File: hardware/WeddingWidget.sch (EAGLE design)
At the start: 7 parts, among them J1 AVR_SPI_PRG_6NS, SW1 EVQQ2, SW2 EVQQ2

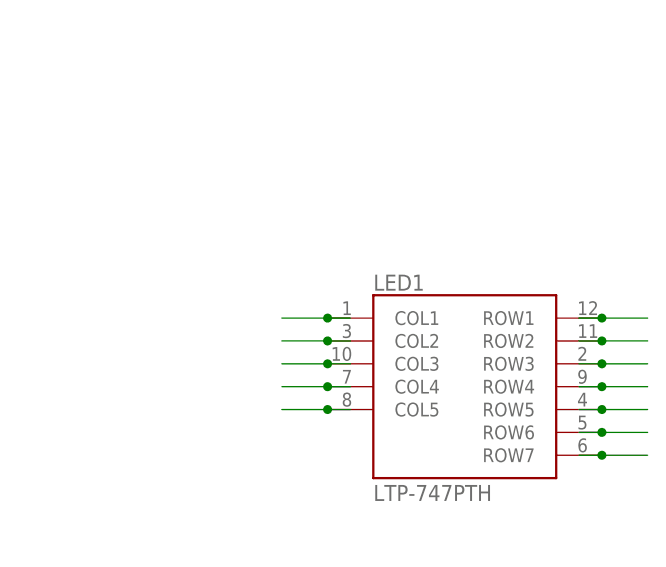
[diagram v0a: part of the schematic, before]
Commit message: added battery holder and bottom ground plane
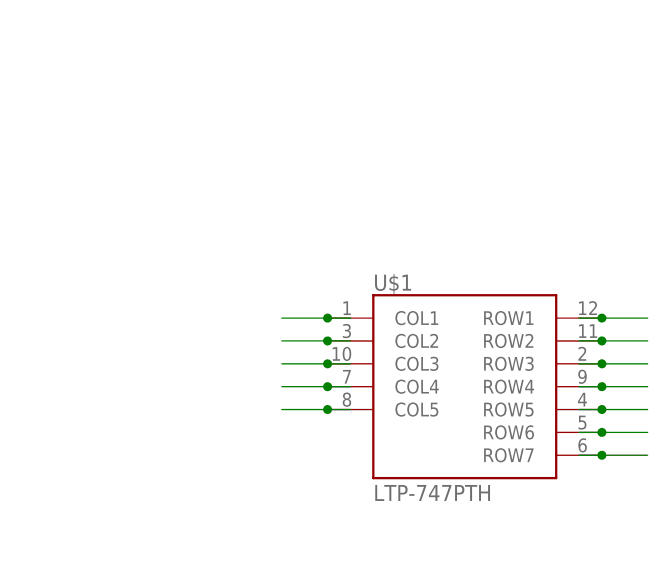
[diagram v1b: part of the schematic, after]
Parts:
- BAT1: device SparkFun:BATTERY12MM -> rxtx-labs:BATTERY12MM
- renumbered LED1 to U$1
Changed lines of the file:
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@@
 <part name="SW1" library="adafruit" deviceset="EVQQ2" device=""/>
 <part name="J1" library="SparkFun" deviceset="AVR_SPI_PRG_6" device="NS"/>
-<part name="BAT1" library="SparkFun" deviceset="BATTERY" device="12MM"/>
-<part name="LED1" library="LiteOn-LED-Matrix" deviceset="LTP-747" device="PTH"/>
 <part name="SW2" library="adafruit" deviceset="EVQQ2" device=""/>
+<part name="BAT1" library="rxtx-labs" deviceset="BATTERY" device="12MM"/>
+<part name="U$1" library="LiteOn-LED-Matrix" deviceset="LTP-747" device="PTH"/>
 </parts>
 <sheets>
@@
 <instance part="SW1" gate="G$1" x="25.4" y="193.04" rot="R270"/>
 <instance part="J1" gate="G$1" x="83.82" y="236.22"/>
+<instance part="SW2" gate="G$1" x="25.4" y="167.64" rot="R270"/>
 <instance part="BAT1" gate="G$1" x="33.02" y="226.06"/>
-<instance part="LED1" gate="G$1" x="182.88" y="175.26"/>
-<instance part="SW2" gate="G$1" x="25.4" y="167.64" rot="R270"/>
+<instance part="U$1" gate="G$1" x="182.88" y="175.26"/>
 </instances>
 <busses>
@@
 <segment>
 <wire x1="170.18" y1="182.88" x2="167.64" y2="182.88" width="0.1524" layer="91"/>
-<pinref part="LED1" gate="G$1" pin="COL1"/>
+<pinref part="U$1" gate="G$1" pin="COL1"/>
 <wire x1="167.64" y1="182.88" x2="162.56" y2="182.88" width="0.1524" layer="91"/>
 <junction x="167.64" y="182.88"/>
@@
 <segment>
 <wire x1="170.18" y1="180.34" x2="167.64" y2="180.34" width="0.1524" layer="91"/>
-<pinref part="LED1" gate="G$1" pin="COL2"/>
+<pinref part="U$1" gate="G$1" pin="COL2"/>
 <wire x1="167.64" y1="180.34" x2="162.56" y2="180.34" width="0.1524" layer="91"/>
 <junction x="167.64" y="180.34"/>
@@
 <segment>
 <wire x1="170.18" y1="177.8" x2="167.64" y2="177.8" width="0.1524" layer="91"/>
-<pinref part="LED1" gate="G$1" pin="COL3"/>
+<pinref part="U$1" gate="G$1" pin="COL3"/>
 <wire x1="167.64" y1="177.8" x2="162.56" y2="177.8" width="0.1524" layer="91"/>
 <junction x="167.64" y="177.8"/>
@@
 <segment>
 <wire x1="170.18" y1="175.26" x2="167.64" y2="175.26" width="0.1524" layer="91"/>
-<pinref part="LED1" gate="G$1" pin="COL4"/>
+<pinref part="U$1" gate="G$1" pin="COL4"/>
 <wire x1="167.64" y1="175.26" x2="162.56" y2="175.26" width="0.1524" layer="91"/>
 <junction x="167.64" y="175.26"/>
@@
 <segment>
 <wire x1="170.18" y1="172.72" x2="167.64" y2="172.72" width="0.1524" layer="91"/>
-<pinref part="LED1" gate="G$1" pin="COL5"/>
+<pinref part="U$1" gate="G$1" pin="COL5"/>
 <wire x1="167.64" y1="172.72" x2="162.56" y2="172.72" width="0.1524" layer="91"/>
 <junction x="167.64" y="172.72"/>
@@
 <segment>
 <wire x1="195.58" y1="182.88" x2="198.12" y2="182.88" width="0.1524" layer="91"/>
-<pinref part="LED1" gate="G$1" pin="ROW1"/>
+<pinref part="U$1" gate="G$1" pin="ROW1"/>
 <wire x1="198.12" y1="182.88" x2="203.2" y2="182.88" width="0.1524" layer="91"/>
 <junction x="198.12" y="182.88"/>
@@
 <segment>
 <wire x1="195.58" y1="180.34" x2="198.12" y2="180.34" width="0.1524" layer="91"/>
-<pinref part="LED1" gate="G$1" pin="ROW2"/>
+<pinref part="U$1" gate="G$1" pin="ROW2"/>
 <wire x1="198.12" y1="180.34" x2="203.2" y2="180.34" width="0.1524" layer="91"/>
 <junction x="198.12" y="180.34"/>
@@
 <segment>
 <wire x1="195.58" y1="177.8" x2="198.12" y2="177.8" width="0.1524" layer="91"/>
-<pinref part="LED1" gate="G$1" pin="ROW3"/>
+<pinref part="U$1" gate="G$1" pin="ROW3"/>
 <wire x1="198.12" y1="177.8" x2="203.2" y2="177.8" width="0.1524" layer="91"/>
 <junction x="198.12" y="177.8"/>
@@
 <segment>
 <wire x1="195.58" y1="175.26" x2="198.12" y2="175.26" width="0.1524" layer="91"/>
-<pinref part="LED1" gate="G$1" pin="ROW4"/>
+<pinref part="U$1" gate="G$1" pin="ROW4"/>
 <wire x1="198.12" y1="175.26" x2="203.2" y2="175.26" width="0.1524" layer="91"/>
 <junction x="198.12" y="175.26"/>
@@
 <segment>
 <wire x1="195.58" y1="172.72" x2="198.12" y2="172.72" width="0.1524" layer="91"/>
-<pinref part="LED1" gate="G$1" pin="ROW5"/>
+<pinref part="U$1" gate="G$1" pin="ROW5"/>
 <wire x1="198.12" y1="172.72" x2="203.2" y2="172.72" width="0.1524" layer="91"/>
 <junction x="198.12" y="172.72"/>
@@
 <segment>
 <wire x1="195.58" y1="170.18" x2="198.12" y2="170.18" width="0.1524" layer="91"/>
-<pinref part="LED1" gate="G$1" pin="ROW6"/>
+<pinref part="U$1" gate="G$1" pin="ROW6"/>
 <wire x1="198.12" y1="170.18" x2="203.2" y2="170.18" width="0.1524" layer="91"/>
 <junction x="198.12" y="170.18"/>
@@
 <segment>
 <wire x1="195.58" y1="167.64" x2="198.12" y2="167.64" width="0.1524" layer="91"/>
-<pinref part="LED1" gate="G$1" pin="ROW7"/>
+<pinref part="U$1" gate="G$1" pin="ROW7"/>
 <wire x1="198.12" y1="167.64" x2="203.2" y2="167.64" width="0.1524" layer="91"/>
 <junction x="198.12" y="167.64"/>

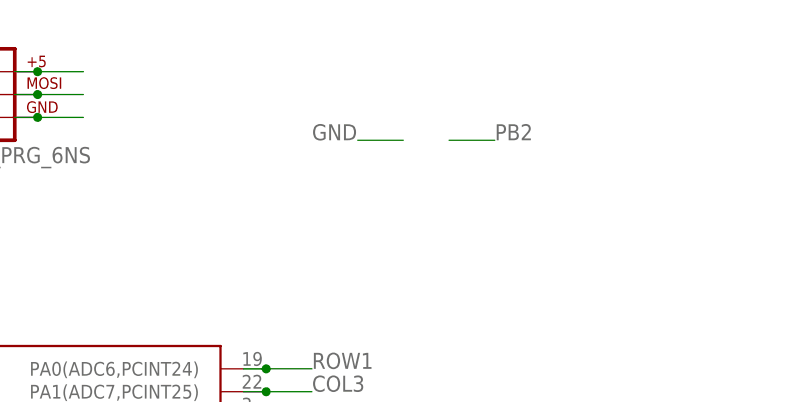
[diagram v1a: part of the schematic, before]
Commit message: Hand routed all traces. Ready for prototype boards to be produced.
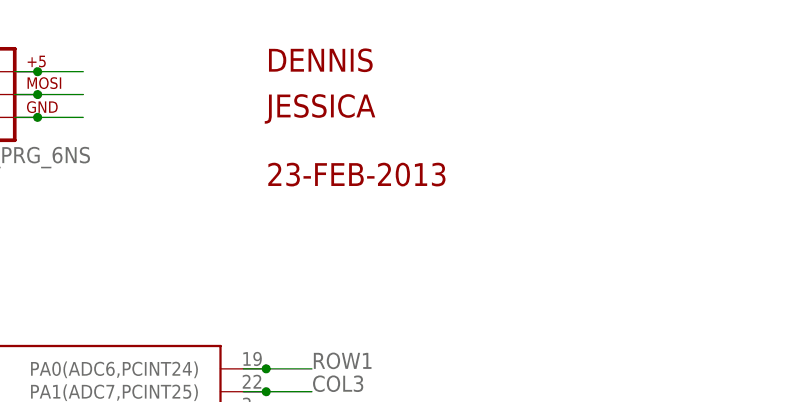
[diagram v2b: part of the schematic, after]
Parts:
- added U$2: DENNIS, rxtx-labs:DENNIS
- added U$3: JESSICA, rxtx-labs:JESSICA
- added U$4: 23FEB2013, rxtx-labs:23FEB2013
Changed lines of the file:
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@@
 <part name="BAT1" library="rxtx-labs" deviceset="BATTERY" device="12MM"/>
 <part name="U$1" library="LiteOn-LED-Matrix" deviceset="LTP-747" device="PTH"/>
+<part name="U$2" library="rxtx-labs" deviceset="DENNIS" device=""/>
+<part name="U$3" library="rxtx-labs" deviceset="JESSICA" device=""/>
+<part name="U$4" library="rxtx-labs" deviceset="23FEB2013" device=""/>
 </parts>
 <sheets>
@@
 <instance part="BAT1" gate="G$1" x="33.02" y="226.06"/>
 <instance part="U$1" gate="G$1" x="182.88" y="175.26"/>
+<instance part="U$2" gate="G$1" x="119.38" y="238.76"/>
+<instance part="U$3" gate="G$1" x="119.38" y="233.68"/>
+<instance part="U$4" gate="G$1" x="119.38" y="226.06"/>
 </instances>
 <busses>
@@
 <junction x="20.32" y="193.04"/>
 <junction x="20.32" y="190.5"/>
-</segment>
-<segment>
-<label x="124.46" y="231.14" size="1.778" layer="95"/>
-<wire x1="134.62" y1="231.14" x2="129.54" y2="231.14" width="0.1524" layer="91"/>
 </segment>
 <segment>
@@
 </segment>
 </net>
-<net name="PB2" class="0">
-<segment>
-<label x="144.78" y="231.14" size="1.778" layer="95"/>
-<wire x1="139.7" y1="231.14" x2="144.78" y2="231.14" width="0.1524" layer="91"/>
-</segment>
-</net>

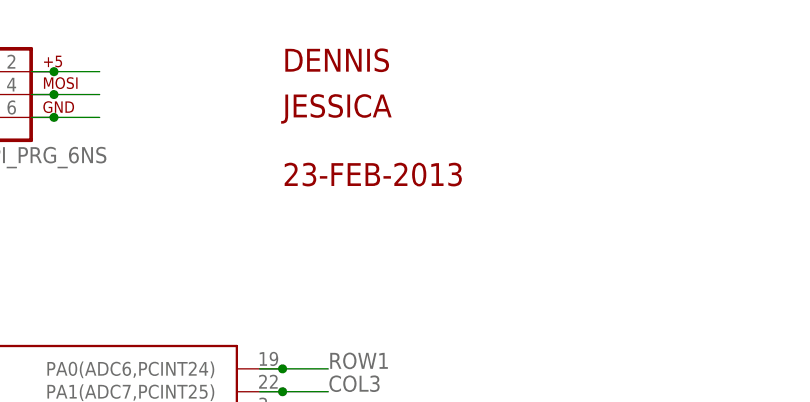
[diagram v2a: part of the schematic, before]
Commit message: Dropped bitmapped text for prototype run.
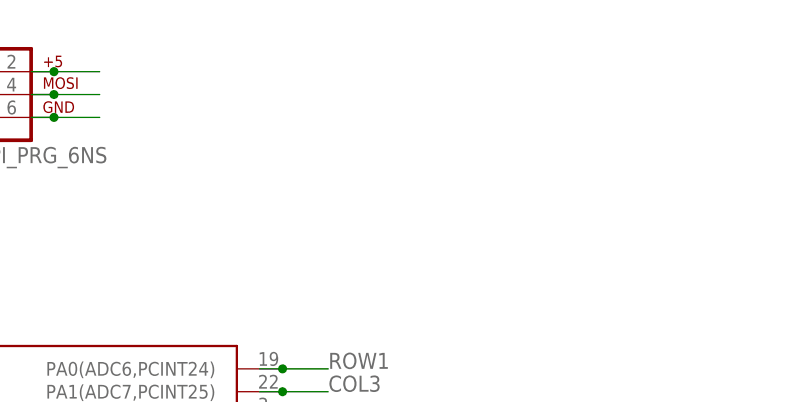
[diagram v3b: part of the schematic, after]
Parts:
- removed U$2: DENNIS, rxtx-labs:DENNIS
- removed U$3: JESSICA, rxtx-labs:JESSICA
- removed U$4: 23FEB2013, rxtx-labs:23FEB2013
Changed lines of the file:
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@@
 <part name="BAT1" library="rxtx-labs" deviceset="BATTERY" device="12MM"/>
 <part name="U$1" library="LiteOn-LED-Matrix" deviceset="LTP-747" device="PTH"/>
-<part name="U$2" library="rxtx-labs" deviceset="DENNIS" device=""/>
-<part name="U$3" library="rxtx-labs" deviceset="JESSICA" device=""/>
-<part name="U$4" library="rxtx-labs" deviceset="23FEB2013" device=""/>
 </parts>
 <sheets>
@@
 <instance part="BAT1" gate="G$1" x="33.02" y="226.06"/>
 <instance part="U$1" gate="G$1" x="182.88" y="175.26"/>
-<instance part="U$2" gate="G$1" x="119.38" y="238.76"/>
-<instance part="U$3" gate="G$1" x="119.38" y="233.68"/>
-<instance part="U$4" gate="G$1" x="119.38" y="226.06"/>
 </instances>
 <busses>

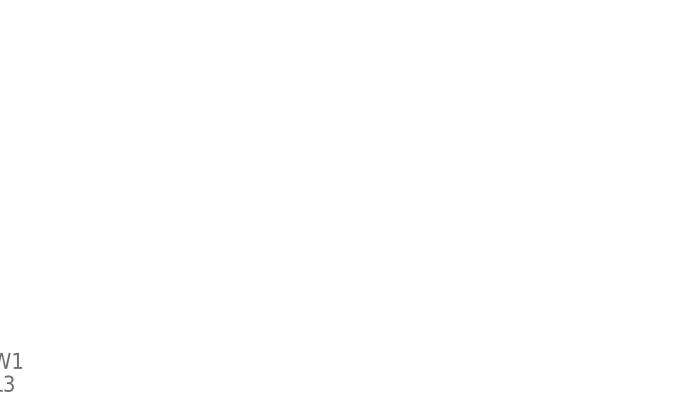
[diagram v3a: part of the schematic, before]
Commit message: added bitmap text to board
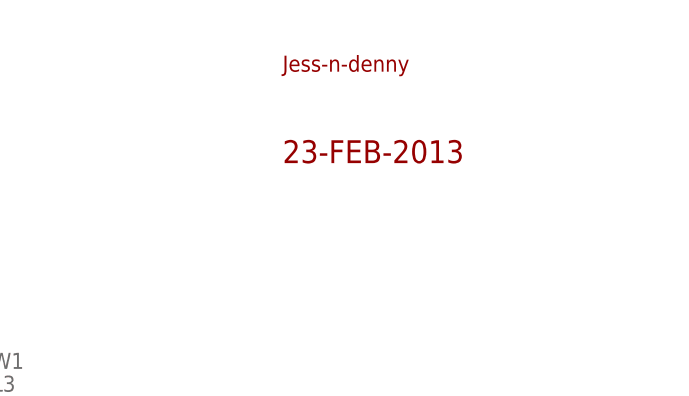
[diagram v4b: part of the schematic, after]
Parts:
- added U$2: JESS-N-DENNY, rxtx-labs:JESS-N-DENNY
- added U$3: 23FEB2013, rxtx-labs:23FEB2013
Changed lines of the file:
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@@
 <part name="BAT1" library="rxtx-labs" deviceset="BATTERY" device="12MM"/>
 <part name="U$1" library="LiteOn-LED-Matrix" deviceset="LTP-747" device="PTH"/>
+<part name="U$2" library="rxtx-labs" deviceset="JESS-N-DENNY" device=""/>
+<part name="U$3" library="rxtx-labs" deviceset="23FEB2013" device=""/>
 </parts>
 <sheets>
@@
 <instance part="BAT1" gate="G$1" x="33.02" y="226.06"/>
 <instance part="U$1" gate="G$1" x="182.88" y="175.26"/>
+<instance part="U$2" gate="G$1" x="160.02" y="238.76"/>
+<instance part="U$3" gate="G$1" x="160.02" y="228.6"/>
 </instances>
 <busses>

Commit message: Final design. Sent for manufacturing.
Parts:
- added U$4: HEART, rxtx-labs:HEART
- added U$5: TETRISH, rxtx-labs:TETRISH
- added U$6: TRIFORCE, rxtx-labs:TRIFORCE
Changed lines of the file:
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@@
 <part name="U$2" library="rxtx-labs" deviceset="JESS-N-DENNY" device=""/>
 <part name="U$3" library="rxtx-labs" deviceset="23FEB2013" device=""/>
+<part name="U$4" library="rxtx-labs" deviceset="HEART" device=""/>
+<part name="U$5" library="rxtx-labs" deviceset="TETRISH" device=""/>
+<part name="U$6" library="rxtx-labs" deviceset="TRIFORCE" device=""/>
 </parts>
 <sheets>
@@
 <instance part="U$2" gate="G$1" x="160.02" y="238.76"/>
 <instance part="U$3" gate="G$1" x="160.02" y="228.6"/>
+<instance part="U$4" gate="G$1" x="162.56" y="218.44"/>
+<instance part="U$5" gate="G$1" x="203.2" y="238.76"/>
+<instance part="U$6" gate="G$1" x="203.2" y="226.06"/>
 </instances>
 <busses>
